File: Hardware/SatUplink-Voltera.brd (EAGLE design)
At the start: 55 x 68 mm, 40 parts, among them U1 MIC5219-3.3, U2 AP7311-1.8, U3 74HC4050, U4 SPOT-CONNECT, U5 ARDUINO_SHIELD, U6 MIC5219-3.0, U7 MIC5219-3.0

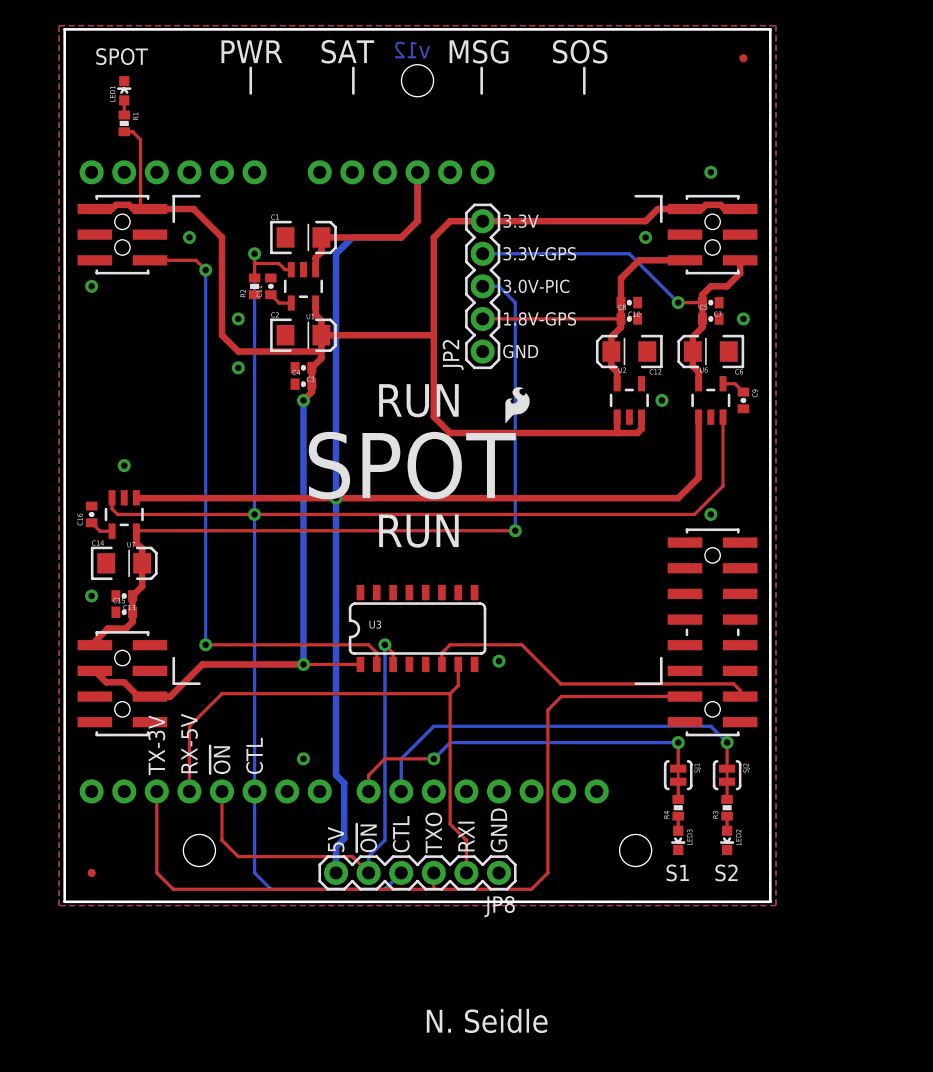
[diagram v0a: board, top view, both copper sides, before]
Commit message: Voltera Edits
The V12 board has been edited to fit onto the Voltera Arduino Uno
substrate board.
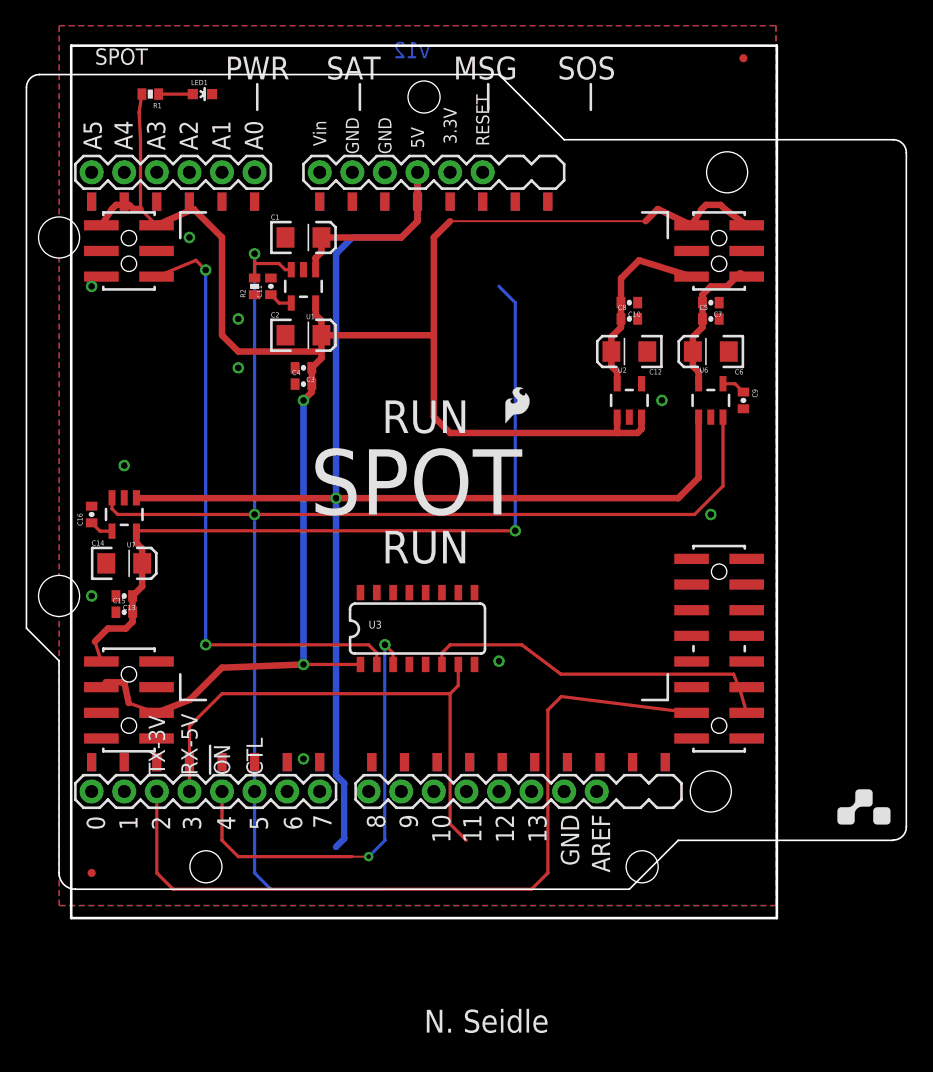
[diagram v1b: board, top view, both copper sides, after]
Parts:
- removed JP2: (no value), SparkFun:1X05
- removed JP8: (no value), SparkFun:1X06
- removed LED2: Blue, SparkFun:LED-0603
- removed LED3: Green, SparkFun:LED-0603
- removed R3, R4: 330, SparkFun:0402-RES
- removed SJ1, SJ2: (no value), SparkFun:SJ_2S-TRACE
- added U$4: TEMPLATE_ARDUINO_UNO_SHIELD, voltera_EAGLE_community_lib:ARDUINO_UNO
- U3: value 74HC4050 -> 74HC5040
- moved U$3 16.4 mm to (41.7, 21.1)
- moved LED1 6.10 mm to (10.7, 63.0), turned to 270 degrees
- moved R1 3.06 mm to (6.60, 63.0), turned to 180 degrees
- moved U4 1.37 mm to (27.9, 32.8)
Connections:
- removed net N$2: R4.2, SJ1.2
- removed net N$3: R3.2, SJ2.2
- removed net N$5: LED2.A, R3.1
- removed net N$6: LED3.A, R4.1
- net !ON-5V: now also U$4.4@1, U$4.4@2; no longer JP8.5
- net 1.8V-GPS: no longer JP2.2
- net 3.3V: no longer JP2.5
- net 3V-GPS: no longer JP2.4
- net 3V-PIC: no longer JP2.3
- net 5V: now also U$4.5V@1, U$4.5V@2; no longer JP8.6
- net GND: now also U$4.GND..@1, U$4.GND..@2, U$4.GND.@1, U$4.GND.@2, U$4.GND@1, U$4.GND@2, U5.D11; no longer JP2.1, JP8.1, LED2.C, LED3.C
- net N$7: now also U$4.8@1, U$4.8@2; no longer SJ1.1
- net N$8: now also U$4.9@1, U$4.9@2; no longer SJ2.1
- net PWRCTL: now also U$4.5@1, U$4.5@2; no longer JP8.4
- net SPOT-RX-5V: now also U$4.3@1, U$4.3@2; no longer JP8.2
- net SPOT-TX-3V: now also U$4.2@1, U$4.2@2; no longer JP8.3
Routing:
- net N$8: track 31.6 -> 0.00 mm, vias 1 -> 0
- net N$7: track 28.5 -> 0.00 mm, vias 2 -> 0
- net 3V-GPS: track 30.8 -> 11.6 mm, vias 1 -> 0
- net 1.8V-GPS: track 25.1 -> 15.0 mm
- net 3.3V: track 152.3 -> 157.7 mm
- net SPOT-RX-5V: track 43.5 -> 41.0 mm
- net 5V: track 123.7 -> 121.7 mm
- net !ON-5V: track 36.4 -> 34.6 mm, vias 1 -> 2
- net PWRCTL: track 120.6 -> 118.8 mm
- net N$38: track 1.14 -> 2.66 mm
- net SPOT-RX-3V: track 26.3 -> 27.8 mm
- net N$3: track 1.38 -> 0.00 mm
- net N$2: track 1.38 -> 0.00 mm
- net N$6: track 1.14 -> 0.00 mm
- net N$5: track 1.14 -> 0.00 mm
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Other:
- board size 55 x 68 mm -> 68.6 x 63.5 mm
- board text removed: "1.8V-GPS"
- board text removed: "3.0V-PIC"
- board text removed: "3.3V"
- board text removed: "3.3V-GPS"
- board text removed: "5V"
- board text removed: "GND"
- board text removed: "RXI"
- board text removed: "S1"
- board text removed: "S2"
- board text removed: "TXO"
